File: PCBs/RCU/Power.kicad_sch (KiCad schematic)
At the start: 3 parts

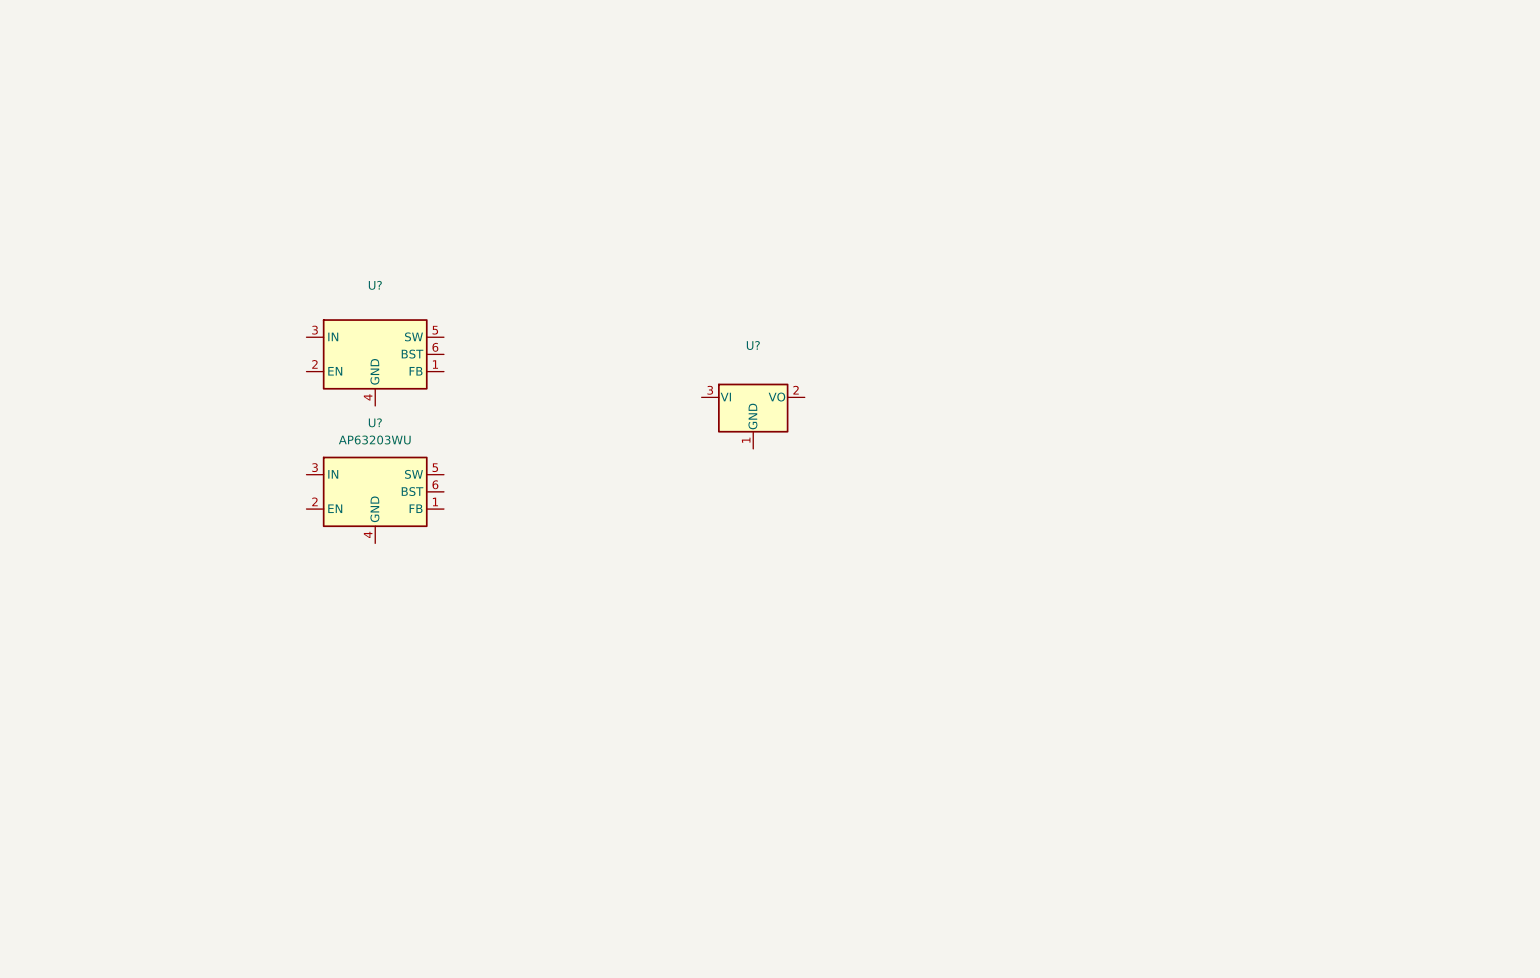
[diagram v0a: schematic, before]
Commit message: Finished Power module with power selector
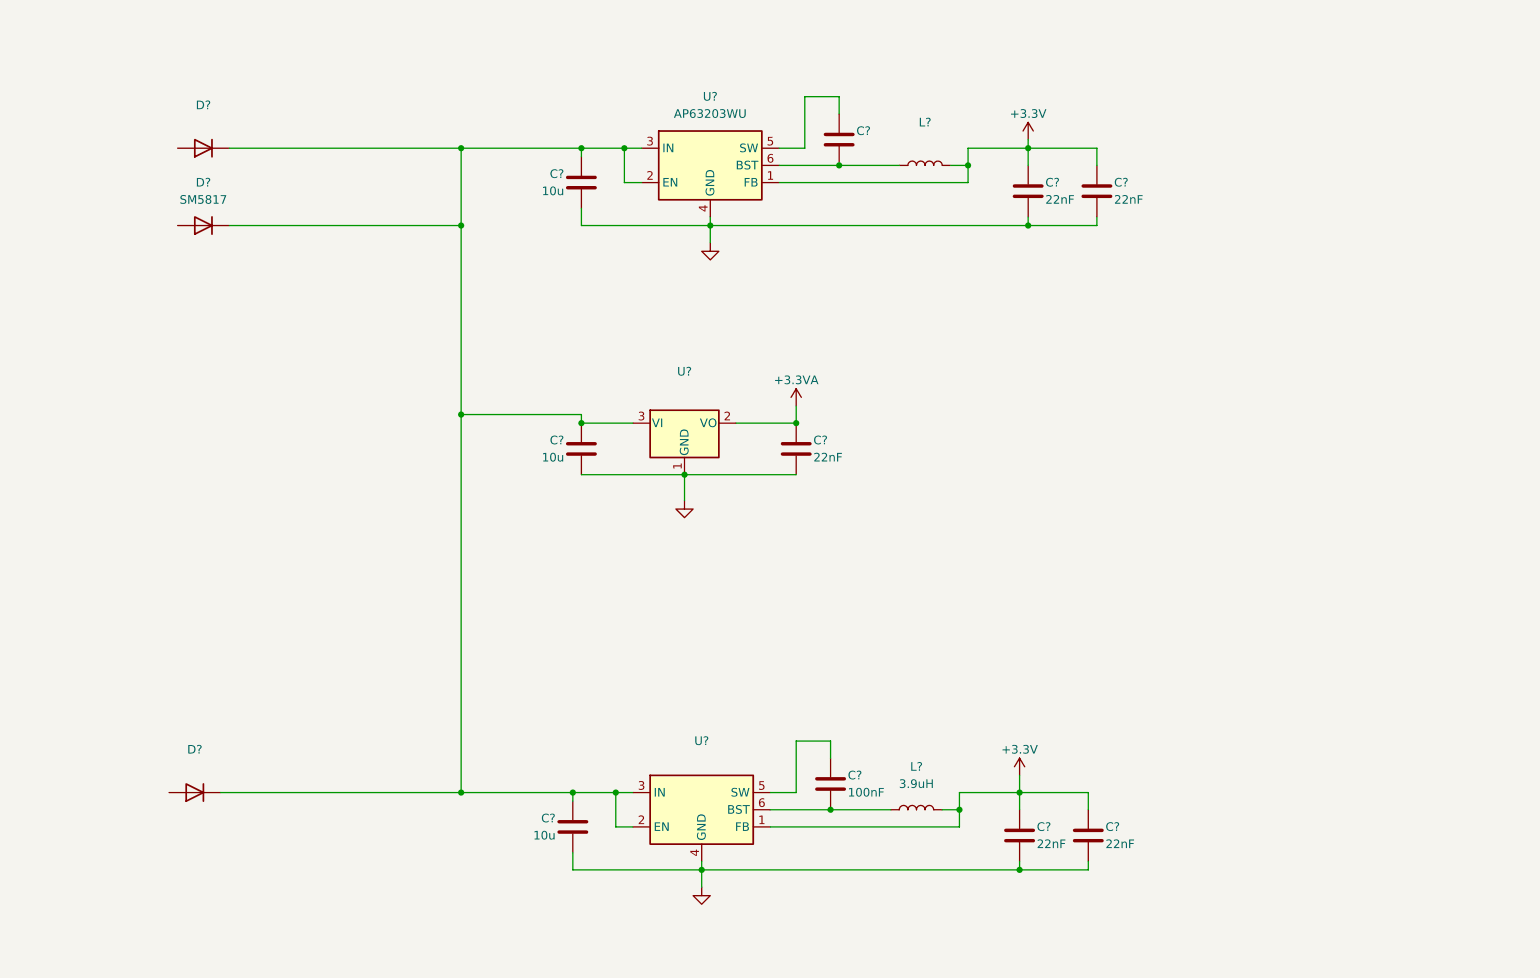
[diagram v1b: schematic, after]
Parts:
- added C? (x3): 10u, symbol Device:C
- added C? (x5): 22nF, symbol Device:C
- added C?: (no value), symbol Device:C
- added C?: 100nF, symbol Device:C
- added D?: (no value), symbol Diode:1N4148W
- added D?: (no value), symbol Diode:SM513
- added D?: SM5817, symbol Diode:SM513
- added L?: (no value), symbol Device:L
- added L?: 3.9uH, symbol Device:L
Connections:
- net +3V3: now reaches U?.1 (FB)
- net +3V3: now also U?.1 (FB), C?.1, C?.1, C?.1, C?.1, L?.2, L?.2
- net at U?.2 (EN): now also U?.2 (EN), U?.3 (IN), U?.3 (IN), U?.3 (VI), C?.1, C?.1, C?.1, D?.1 (K), D?.1 (K), D?.1 (K)
- net GND: now reaches U?.4 (GND)
- net GND: now also U?.1 (GND), U?.4 (GND), C?.2, C?.2, C?.2, C?.2, C?.2, C?.2, C?.2, C?.2
- net at U?.5 (SW): now also C?.1 (x2)
- net at U?.6 (BST): now also C?.2, L?.1 (x2)
- net +3.3VA: now reaches U?.2 (VO)
- net +3.3VA: now also C?.1
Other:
- moved on the sheet: U?

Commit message: Used appropriate names for UART signals
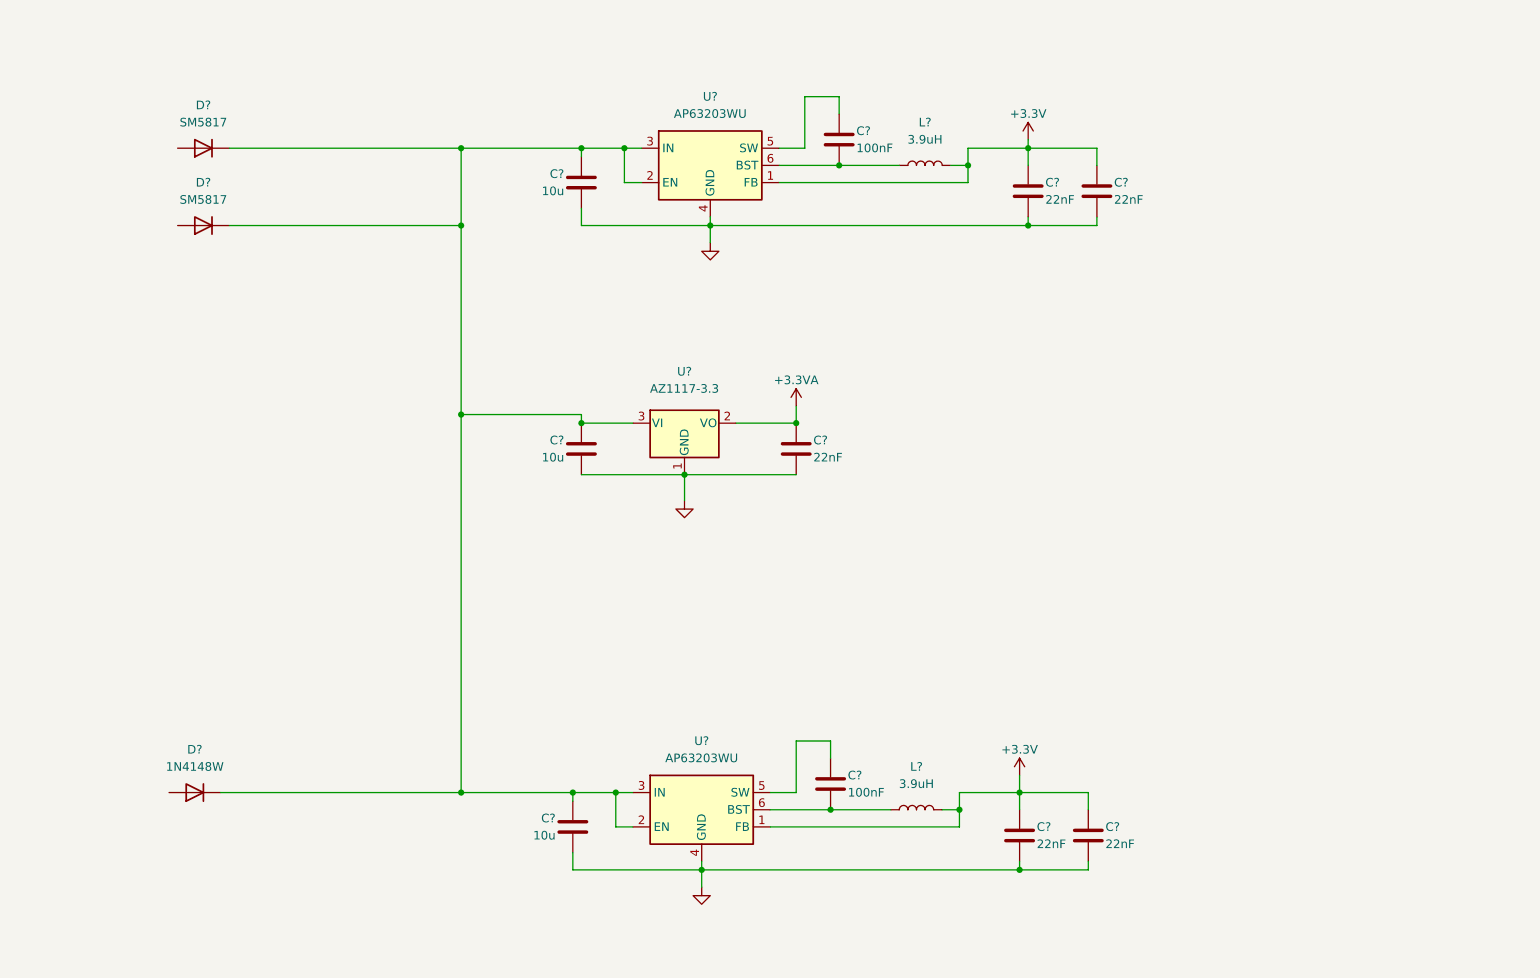
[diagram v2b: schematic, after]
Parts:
- C?: value (none) -> 100nF
- D?: value (none) -> 1N4148W; footprint (none) -> Diode_SMD:D_SOD-123
- D?: value (none) -> SM5817
- L?: value (none) -> 3.9uH
- U?: value (none) -> AZ1117-3.3
- U?: value (none) -> AP63203WU; footprint (none) -> Package_TO_SOT_SMD:TSOT-23-6
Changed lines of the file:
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@@
     (in_bom yes) (on_board yes) (fields_autoplaced)
     (property "Reference" "D?" (id 0) (at 52.07 128.27 0))
-    (property "Value" "" (id 1) (at 52.07 130.81 0))
-    (property "Footprint" "" (id 2) (at 52.07 130.175 0)
+    (property "Value" "1N4148W" (id 1) (at 52.07 130.81 0))
+    (property "Footprint" "Diode_SMD:D_SOD-123" (id 2) (at 52.07 130.175 0)
       (effects (font (size 1.27 1.27)) hide)
     )
@@
     (in_bom yes) (on_board yes) (fields_autoplaced)
     (property "Reference" "U?" (id 0) (at 124.46 72.39 0))
-    (property "Value" "" (id 1) (at 124.46 74.93 0))
+    (property "Value" "AZ1117-3.3" (id 1) (at 124.46 74.93 0))
     (property "Footprint" "" (id 2) (at 124.46 73.66 0)
       (effects (font (size 1.27 1.27) italic) hide)
@@
     (in_bom yes) (on_board yes) (fields_autoplaced)
     (property "Reference" "L?" (id 0) (at 160.02 35.56 90))
-    (property "Value" "" (id 1) (at 160.02 38.1 90))
+    (property "Value" "3.9uH" (id 1) (at 160.02 38.1 90))
     (property "Footprint" "" (id 2) (at 160.02 41.91 0)
       (effects (font (size 1.27 1.27)) hide)
@@
     (in_bom yes) (on_board yes) (fields_autoplaced)
     (property "Reference" "D?" (id 0) (at 53.34 33.02 0))
-    (property "Value" "" (id 1) (at 53.34 35.56 0))
+    (property "Value" "SM5817" (id 1) (at 53.34 35.56 0))
     (property "Footprint" "" (id 2) (at 53.34 34.925 0)
       (effects (font (size 1.27 1.27)) hide)
@@
     (in_bom yes) (on_board yes) (fields_autoplaced)
     (property "Reference" "U?" (id 0) (at 127 127 0))
-    (property "Value" "" (id 1) (at 127 129.54 0))
-    (property "Footprint" "" (id 2) (at 127 160.02 0)
+    (property "Value" "AP63203WU" (id 1) (at 127 129.54 0))
+    (property "Footprint" "Package_TO_SOT_SMD:TSOT-23-6" (id 2) (at 127 160.02 0)
       (effects (font (size 1.27 1.27)) hide)
     )
@@
       (effects (font (size 1.27 1.27)) (justify left))
     )
-    (property "Value" "" (id 1) (at 149.86 39.37 0)
+    (property "Value" "100nF" (id 1) (at 149.86 39.37 0)
       (effects (font (size 1.27 1.27)) (justify left))
     )

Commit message: Add USB power filter circuitry and corrected Motor Driver schematic
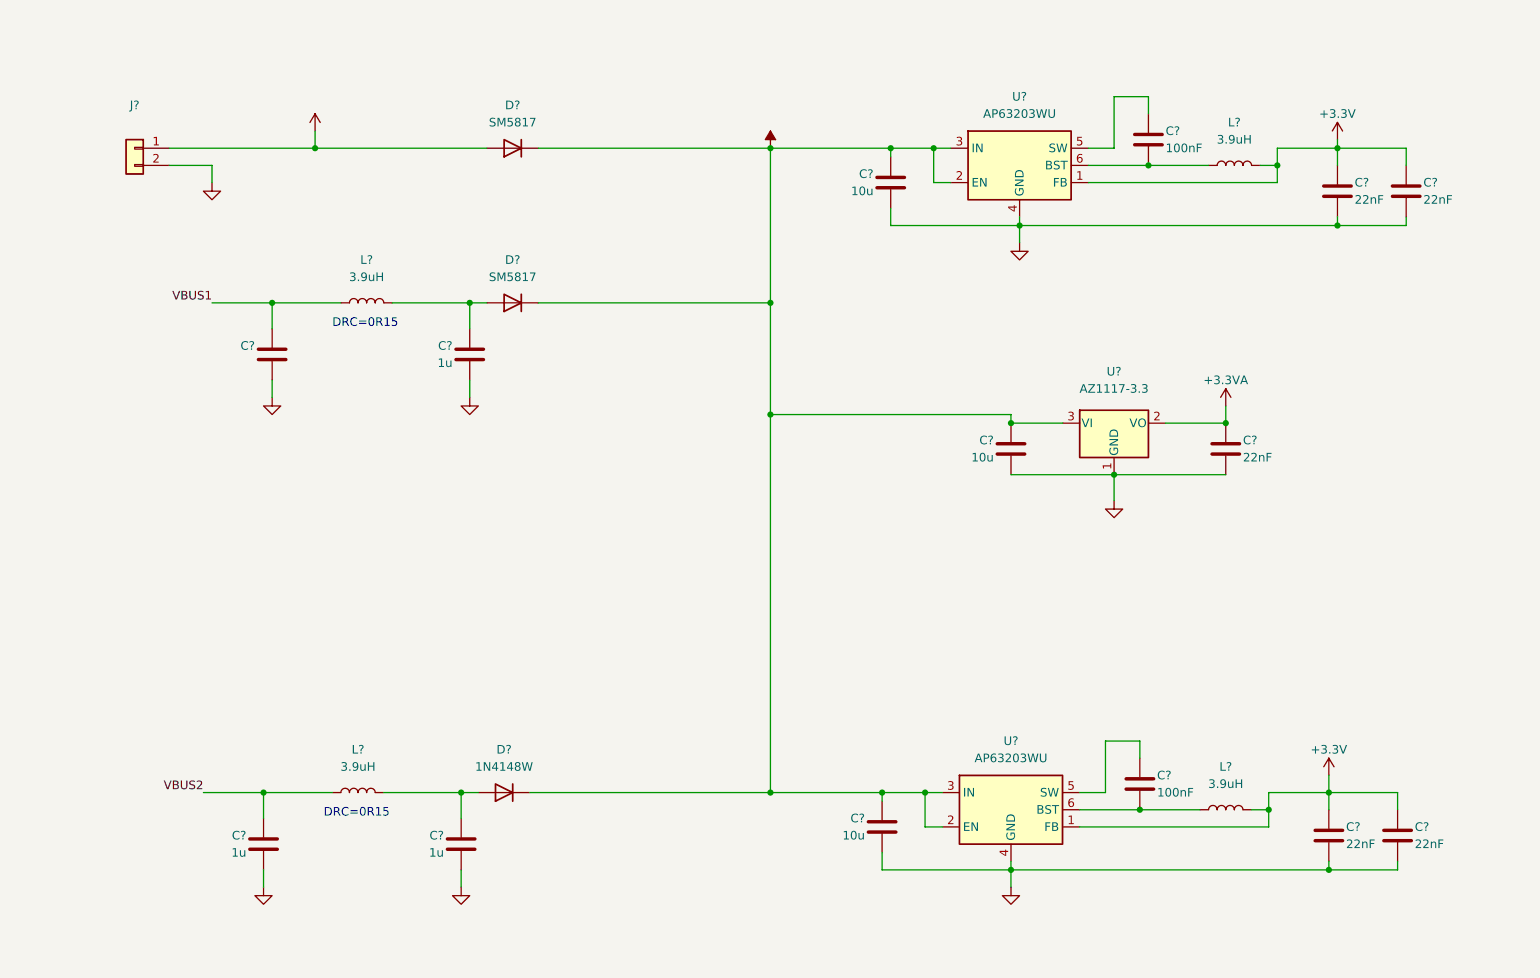
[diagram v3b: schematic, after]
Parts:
- added C? (x3): 1u, symbol Device:C
- added C?: (no value), symbol Device:C
- added J?: (no value), symbol Connector_Generic:Conn_01x02
- added L? (x2): 3.9uH, symbol Device:L
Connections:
- net GND: now also C?.2, C?.2, C?.2, C?.2, J?.2 (Pin_2)
- net VCOM: now reaches C?.1, C?.1, C?.1, D?.1 (K), D?.1 (K), D?.1 (K), U?.2 (EN), U?.2 (EN), U?.3 (IN), U?.3 (IN), U?.3 (VI)
- net at D?.2 (A): now also C?.1, L?.2 (x2)
- net +BATT: now reaches D?.2 (A)
- net +BATT: now also J?.1 (Pin_1)
- new net VBUS1: C?.1, L?.1
- new net VBUS2: C?.1, L?.1
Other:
- note added: "DRC=0R15"
- moved on the sheet: C?, D?, L?, U?

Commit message: Add battery filter circuit, corrected cap values for 3.3V regulators, used different output power floag for Bottom regulator so that it only powers the Bluetooth susbsystem
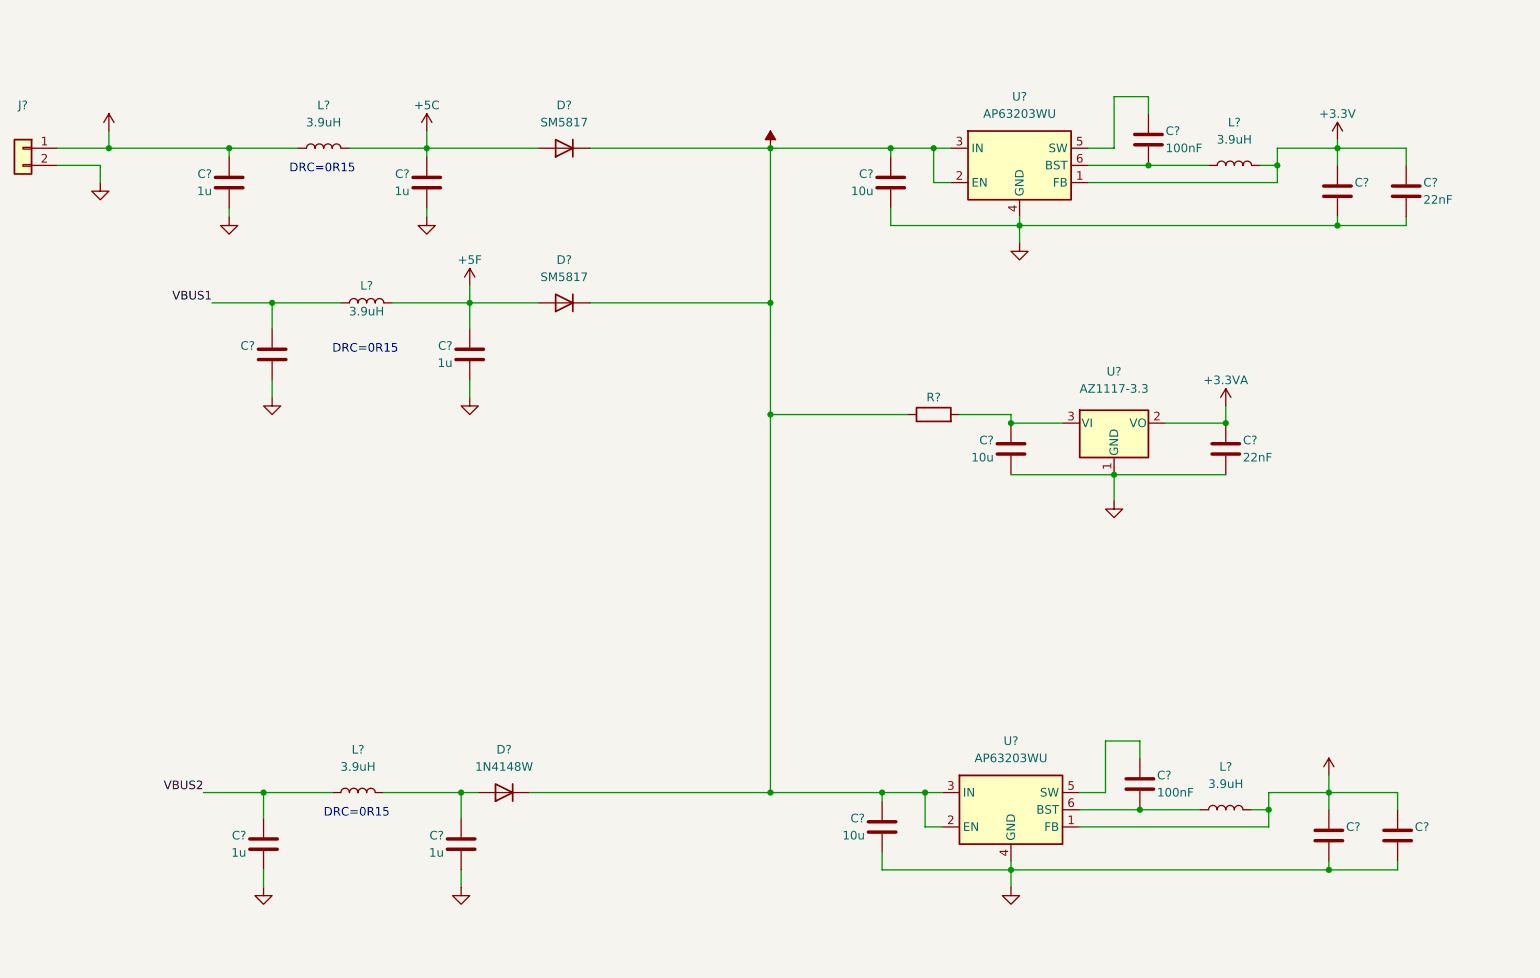
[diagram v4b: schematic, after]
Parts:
- added C? (x2): 1u, symbol Device:C
- added L?: 3.9uH, symbol Device:L
- added R?: (no value), symbol Device:R
- C? (x3): value 22nF -> (none)
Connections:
- net +3V3: no longer C?.1, C?.1, L?.2, U?.1 (FB)
- net +BATT: now also C?.1, L?.1; no longer D?.2 (A)
- net GND: now also C?.2, C?.2
- net VCOM: now also R?.1; no longer C?.1, U?.3 (VI)
- net +5F: now reaches C?.1, D?.2 (A), L?.2
- new net: C?.1, R?.2, U?.3 (VI)
- new net +3.3VP: C?.1, C?.1, L?.2, U?.1 (FB)
- new net +5C: C?.1, D?.2 (A), L?.2
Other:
- moved on the sheet: D?, J?

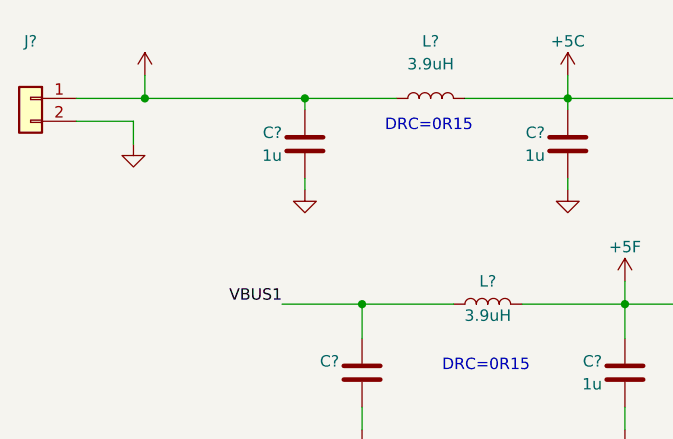
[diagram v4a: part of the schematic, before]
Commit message: Made corrections to Power module and power flag used to power BT susbsystem
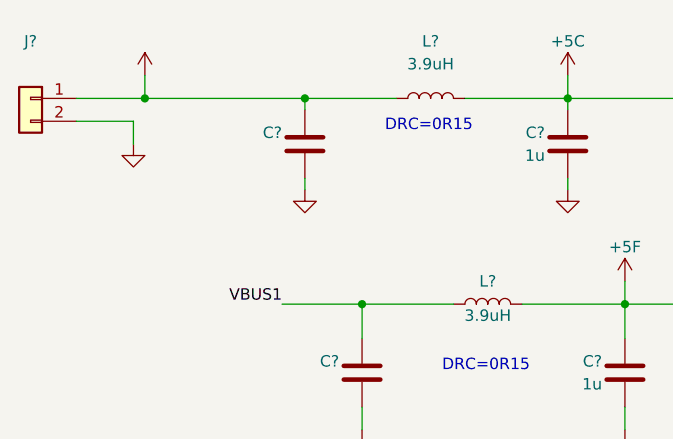
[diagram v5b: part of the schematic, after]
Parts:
- C?: value 1u -> (none)
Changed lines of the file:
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@@
       (effects (font (size 1.27 1.27)) (justify left))
     )
-    (property "Value" "1u" (id 1) (at 54.61 45.72 0)
+    (property "Value" "" (id 1) (at 54.61 45.72 0)
       (effects (font (size 1.27 1.27)) (justify left))
     )
